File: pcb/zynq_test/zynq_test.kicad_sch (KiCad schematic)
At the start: 0 parts

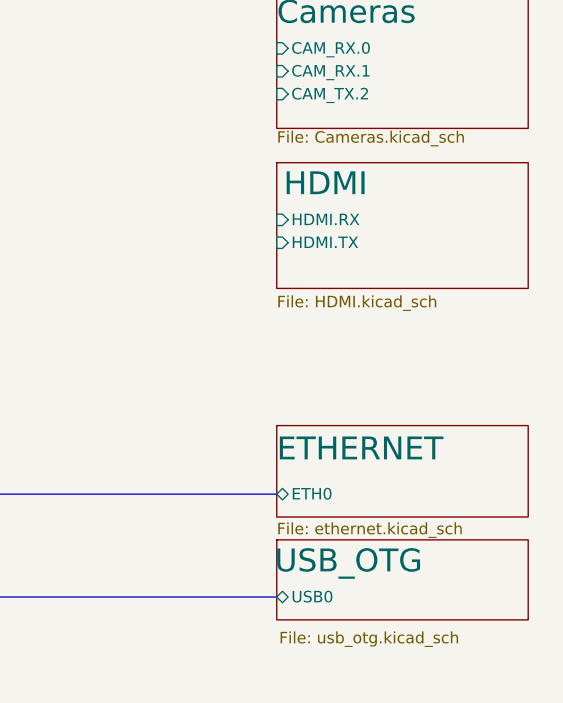
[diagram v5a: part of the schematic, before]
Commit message: Finished HDMI
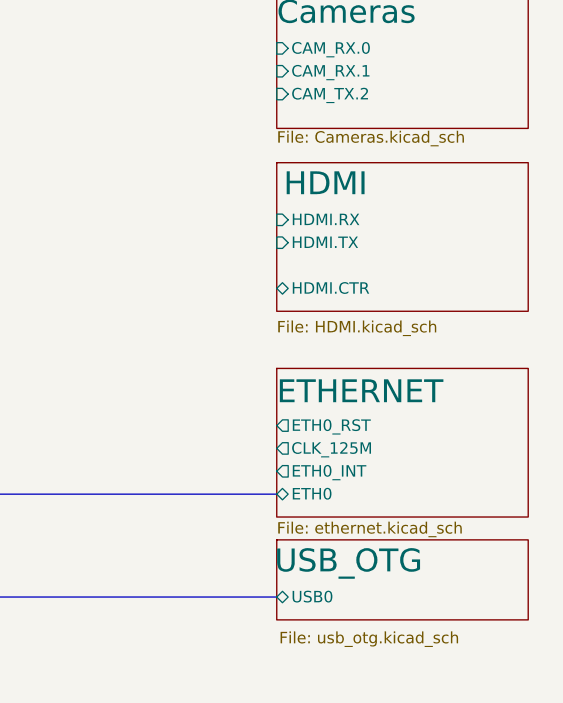
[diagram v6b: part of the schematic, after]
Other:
- sheet ETHERNET ports: added CLK_125M, ETH0_INT, ETH0_RST; removed none
- sheet HDMI ports: added HDMI.CTR; removed none
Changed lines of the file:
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@@
 	(sheet
 		(at 212.09 34.29)
-		(size 27.94 13.97)
+		(size 27.94 16.51)
 		(exclude_from_sim no)
 		(in_bom yes)
@@
 		)
 		(property "Sheetfile" "HDMI.kicad_sch"
-			(at 212.09 49.022 0)
+			(at 212.09 51.816 0)
 			(effects
 				(font
@@
 		(pin "HDMI.TX" input
 			(at 212.09 43.18 180)
+			(effects
+				(font
+					(size 1.27 1.27)
+				)
+				(justify left)
+			)
+		)
+		(pin "HDMI.CTR" bidirectional
+			(at 212.09 48.26 180)
 			(effects
 				(font
@@
 	)
 	(sheet
-		(at 212.09 63.5)
-		(size 27.94 10.16)
+		(at 212.09 57.15)
+		(size 27.94 16.51)
 		(exclude_from_sim no)
 		(in_bom yes)
@@
 		)
 		(property "Sheetname" "ETHERNET"
-			(at 212.09 67.564 0)
+			(at 212.09 61.214 0)
 			(effects
 				(font
@@
 		)
 		(property "Sheetfile" "ethernet.kicad_sch"
-			(at 212.09 74.2446 0)
+			(at 212.09 74.168 0)
 			(effects
 				(font
@@
 			(effects
 				(font
+					(size 1.27 1.27)
+				)
+				(justify left)
+			)
+		)
+		(pin "CLK_125M" output
+			(at 212.09 66.04 180)
+			(effects
+				(font
+					(size 1.27 1.27)
+				)
+				(justify left)
+			)
+		)
+		(pin "ETH0_INT" output
+			(at 212.09 68.58 180)
+			(effects
+				(font
+					(size 1.27 1.27)
+				)
+				(justify left)
+			)
+		)
+		(pin "ETH0_RST" output
+			(at 212.09 63.5 180)
+			(effects
+				(font

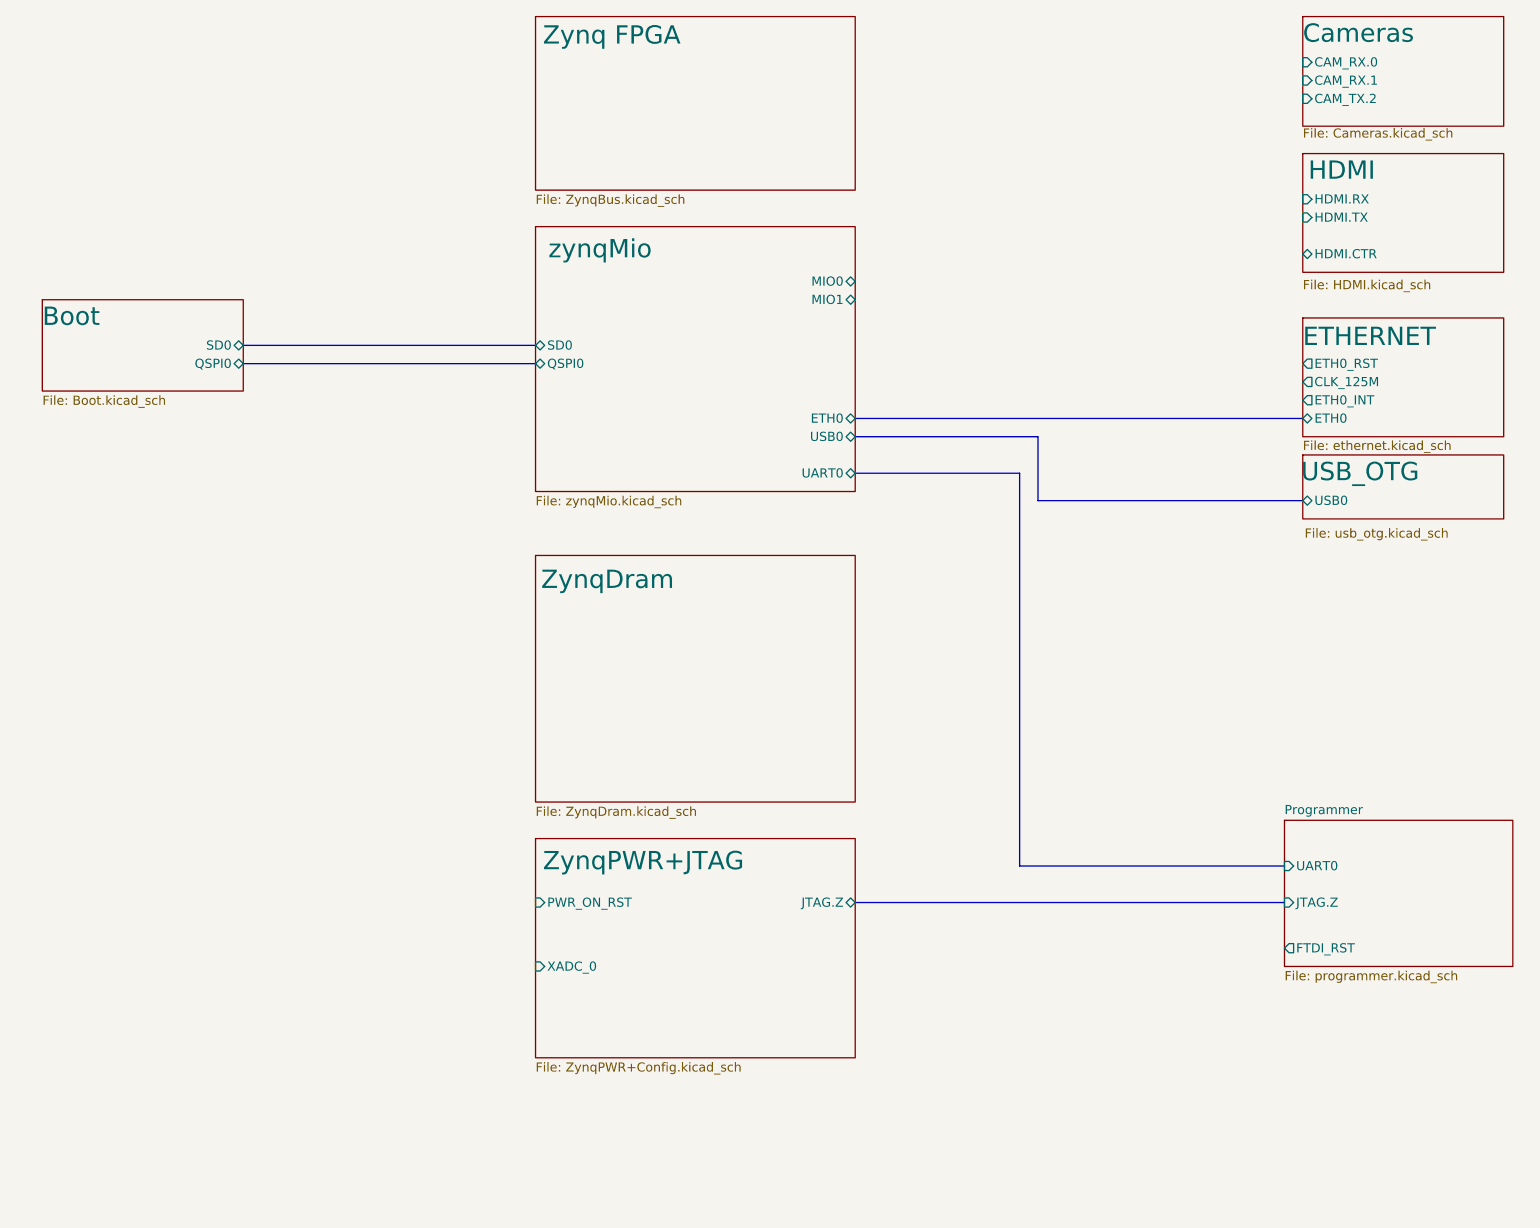
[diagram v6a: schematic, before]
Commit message: Connected DDR3, cleaned up some thing
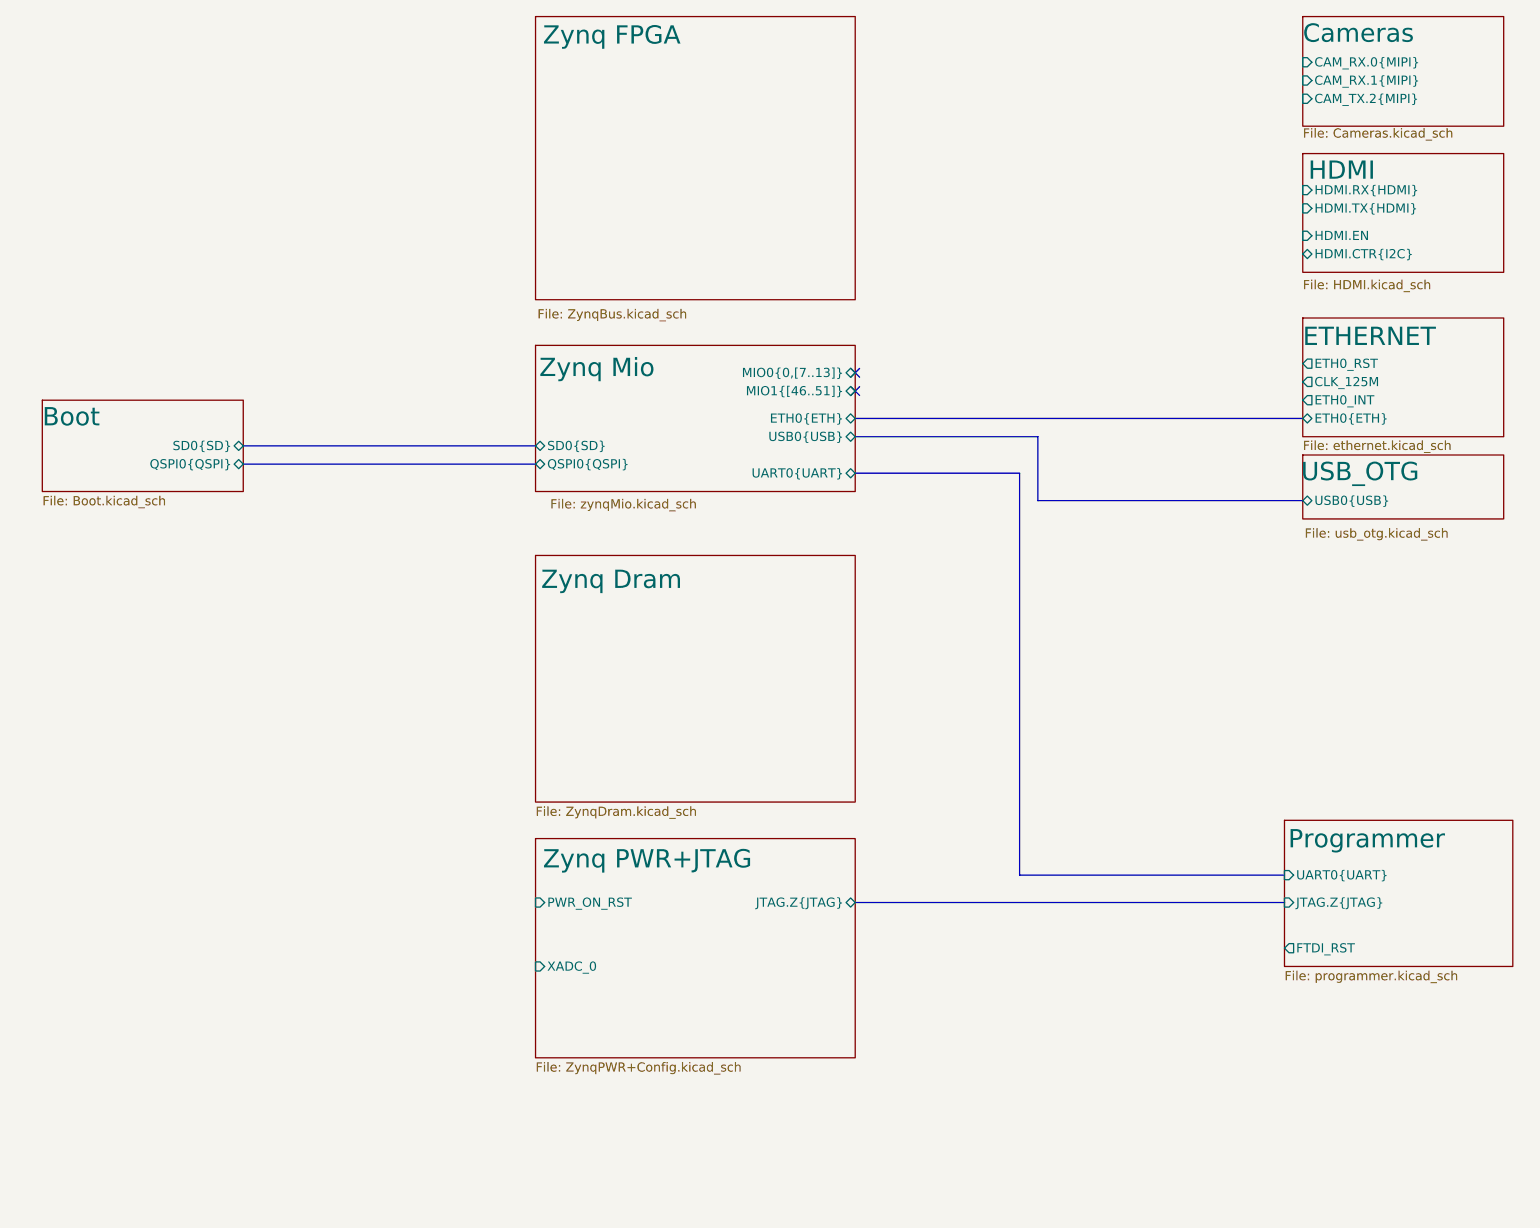
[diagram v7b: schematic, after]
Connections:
- no-connect marks 0 -> 2
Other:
- sheet ZynqDram renamed Zynq Dram
- sheet ZynqPWR+JTAG renamed Zynq PWR+JTAG
- sheet zynqMio renamed Zynq Mio
- sheet Boot ports: added QSPI0{QSPI}, SD0{SD}; removed QSPI0, SD0
- sheet Cameras ports: added CAM_RX.0{MIPI}, CAM_RX.1{MIPI}, CAM_TX.2{MIPI}; removed CAM_RX.0, CAM_RX.1, CAM_TX.2
- sheet ETHERNET ports: added ETH0{ETH}; removed ETH0
- sheet HDMI ports: added HDMI.CTR{I2C}, HDMI.EN, HDMI.RX{HDMI}, HDMI.TX{HDMI}; removed HDMI.CTR, HDMI.RX, HDMI.TX
- sheet Programmer ports: added JTAG.Z{JTAG}, UART0{UART}; removed JTAG.Z, UART0
- sheet USB_OTG ports: added USB0{USB}; removed USB0
- sheet Zynq Mio ports: added ETH0{ETH}, MIO0{0,[7..13]}, MIO1{[46..51]}, QSPI0{QSPI}, SD0{SD}, UART0{UART}, USB0{USB}; removed ETH0, MIO0, MIO1, QSPI0, SD0, UART0, USB0
- sheet Zynq PWR+JTAG ports: added JTAG.Z{JTAG}; removed JTAG.Z

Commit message: Finished Power Supply
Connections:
- no-connect marks 2 -> 15
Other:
- added sheet GPIO (GPIO.kicad_sch)
- added sheet Power (Power.kicad_sch)
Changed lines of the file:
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@@
 	(paper "A4")
 	(title_block
-		(date "2025-09-06")
-		(rev "v1.0")
+		(date "2025-09-13")
+		(rev "A")
+	)
+	(no_connect
+		(at 212.09 41.91)
 	)
 	(no_connect
@@
 	)
 	(no_connect
+		(at 212.09 82.55)
+	)
+	(no_connect
+		(at 209.55 144.78)
+	)
+	(no_connect
+		(at 212.09 48.26)
+	)
+	(no_connect
+		(at 212.09 45.72)
+	)
+	(no_connect
+		(at 212.09 85.09)
+	)
+	(no_connect
 		(at 149.86 64.77)
 	)
-	(bus
-		(pts
-			(xy 175.26 82.55) (xy 175.26 73.66)
+	(no_connect
+		(at 212.09 87.63)
+	)
+	(no_connect
+		(at 105.41 138.43)
+	)
+	(no_connect
+		(at 212.09 39.37)
+	)
+	(no_connect
+		(at 212.09 21.59)
+	)
+	(no_connect
+		(at 212.09 26.67)
+	)
+	(no_connect
+		(at 105.41 147.32)
+	)
+	(no_connect
+		(at 212.09 24.13)
+	)
+	(bus
+		(pts
+			(xy 175.26 101.6) (xy 175.26 73.66)
 		)
 		(stroke
@@
 	(bus
 		(pts
+			(xy 177.8 71.12) (xy 149.86 71.12)
+		)
+		(stroke
+			(width 0)
+			(type default)
+		)
+	)
+	(bus
+		(pts
+			(xy 177.8 90.17) (xy 177.8 71.12)
+		)
+		(stroke
+			(width 0)
+			(type default)
+		)
+	)
+	(bus
+		(pts
 			(xy 172.72 78.74) (xy 172.72 134.62)
 		)
@@
 	(bus
 		(pts
-			(xy 149.86 71.12) (xy 212.09 71.12)
+			(xy 177.8 90.17) (xy 212.09 90.17)
 		)
 		(stroke
@@
 	(bus
 		(pts
-			(xy 175.26 82.55) (xy 212.09 82.55)
+			(xy 175.26 101.6) (xy 212.09 101.6)
 		)
 		(stroke
@@
 	)
 	(sheet
+		(at 33.02 130.81)
+		(size 43.18 25.4)
+		(exclude_from_sim no)
+		(in_bom yes)
+		(on_board yes)
+		(dnp no)
+		(fields_autoplaced yes)
+		(stroke
+			(width 0.1524)
+			(type solid)
+		)
+		(fill
+			(color 0 0 0 0.0000)
+		)
+		(property "Sheetname" "Power"
+			(at 33.02 130.0984 0)
+			(effects
+				(font
+					(size 1.27 1.27)
+				)
+				(justify left bottom)
+			)
+		)
+		(property "Sheetfile" "Power.kicad_sch"
+			(at 33.02 156.7946 0)
+			(effects
+				(font
+					(size 1.27 1.27)
+				)
+				(justify left top)
+			)
+		)
+		(instances
+			(project "zynq_test"
+				(path "/0637578d-4ce5-4d31-b973-2de977269ea5"
+					(page "14")
+				)
+			)
+		)
+	)
+	(sheet
 		(at 105.41 90.17)
 		(size 44.45 34.29)
@@
 	)
 	(sheet
+		(at 212.09 55.88)
+		(size 27.94 16.51)
+		(exclude_from_sim no)
+		(in_bom yes)
+		(on_board yes)
+		(dnp no)
+		(stroke
+			(width 0.1524)
+			(type solid)
+		)
+		(fill
+			(color 0 0 0 0.0000)
+		)
+		(property "Sheetname" "GPIO"
+			(at 212.09 59.69 0)
+			(effects
+				(font
+					(size 2.54 2.54)
+				)
+				(justify left bottom)
+			)
+		)
+		(property "Sheetfile" "GPIO.kicad_sch"
+			(at 212.344 72.898 0)
+			(effects
+				(font
+					(size 1.27 1.27)
+				)
+				(justify left top)
+			)
+		)
+		(instances
+			(project "zynq_test"
+				(path "/0637578d-4ce5-4d31-b973-2de977269ea5"
+					(page "13")
+				)
+			)
+		)
+	)
+	(sheet
 		(at 212.09 34.29)
 		(size 27.94 16.51)
@@
 	)
 	(sheet
-		(at 212.09 57.15)
+		(at 212.09 76.2)
 		(size 27.94 16.51)
 		(exclude_from_sim no)
@@
 		)
 		(property "Sheetname" "ETHERNET"
-			(at 212.09 61.214 0)
+			(at 212.09 80.264 0)
 			(effects
 				(font
@@
 		)
 		(property "Sheetfile" "ethernet.kicad_sch"
-			(at 212.09 74.168 0)
+			(at 212.09 93.218 0)
 			(effects
 				(font
@@
 		)
 		(pin "CLK_125M" output
-			(at 212.09 66.04 180)
+			(at 212.09 85.09 180)
 			(effects
 				(font
@@
 		)
 		(pin "ETH0_INT" output
-			(at 212.09 68.58 180)
+			(at 212.09 87.63 180)
 			(effects
 				(font
@@
 		)
 		(pin "ETH0_RST" output
-			(at 212.09 63.5 180)
+			(at 212.09 82.55 180)
 			(effects
 				(font
@@
 		)
 		(pin "ETH0{ETH}" bidirectional
-			(at 212.09 71.12 180)
+			(at 212.09 90.17 180)
 			(effects
 				(font
@@
 	)
 	(sheet
-		(at 212.09 76.2)
+		(at 212.09 95.25)
 		(size 27.94 8.89)
 		(exclude_from_sim no)
@@
 		)
 		(property "Sheetname" "USB_OTG"
-			(at 211.836 80.01 0)
+			(at 211.836 99.06 0)
 			(effects
 				(font
@@
 		)
 		(property "Sheetfile" "usb_otg.kicad_sch"
-			(at 212.344 86.36 0)
+			(at 212.344 105.41 0)
 			(effects
 				(font
@@
 		)
 		(pin "USB0{USB}" bidirectional
-			(at 212.09 82.55 180)
+			(at 212.09 101.6 180)
 			(effects
 				(font
@@
 	)
 	(embedded_fonts no)
+	(embedded_files
+		(file
+			(name "SheetTemplate.kicad_wks")
+			(type worksheet)
+			(data |KLUv/WB+CMUTADbcWSEAtxsWHGQdlqaixJWgMmfh2tCZyKzY5HXQcxNVVbcAEAFQAEoAUgAh/B3O
+				zZO2eDm5A2l+46HBUjm78+AluXhDg5W0/XTHL/kXAICAICR6H6dUVJrqgq4JQ1Vn/F120TkGjFJq
+				1VlbxHfMPioAAoLxQ9KA3Xc/hV/y995Oy9ae1lTKn3i/85Dn7GLG34c9e1afD4dee/j32zvfoCjC
+				ueuqX3QQCH9dGxS9ziktqxXVkhXrz92PVdUO6sT/PIPwP/YCI7dgWNUQKhEUm1A2zqJlNI2MsUFQ
+				BCvtnAp59TWlwqa0S9bQaBiO21CEXvh3jZyzKfuL/rVpc38UeWxtmpmq7el53qRWAfAi3tC2tUcc
+				qmjVAQGB4bqqtZZEPC5Z5aJpD+5SSEsTclJJNtEimyO8ju+G3d82WEteFENIRNUil+1SKXj73Tvc
+				4JAagFvV34Ey3nT2UFexaJWs4qfLgSH2GlG3jGYJdaAhPaUYmhGRJEkKHYBExMSqG7ZnYf/UXeFb
+				IM2oukJWcjKeZVCGjTWMhUy8XDwRWYjHQURb5Ga0hfkSKue0mhx/YX36Cj3i5k7jAIwo2xZhBro3
+				3UJM24YDkwebfhQeFrxa1f4oKusQJ7gFDGksCLsJASZbNhEyv5f8F9N6PInJsbUuBBQRVByoDeFy
+				JevLuxSpJzWMaOipJyqK1lTks6dcoqx3tGoqDQ1idIc0H6qUvHACH/z2BfdoKcFOmzVa7aKX/pxu
+				Us+lXRAQQiqSU4KpmjACDAjkRIe0IQ0F66JHi1cRBg7mMtNBZR4rOUlqRU4GEwnkdE7s7XRoUefq
+				w1j/C89DpJds9CEdA1EF|
+			)
+			(checksum "F72A94913C597F4C21E195BABBAA6AB8")
+		)
+		(file
+			(name "SheetTemplate2.kicad_wks")
+			(type worksheet)
+			(data |KLUv/WB+COUTAJbcWiEAtxsWHGQdlqaixJWgMmfh2tCZyKzY5HXQcxNVVbcAEAFSAEsAVADYC+Hv
+				cG6etMXLyR1I8xsPDZbK2Z0HL8nFGxqspO2nO37JvwAABAQh0fs4paLSVBd0TRiqOuPvsovOMWCU
+				UqvO2iK+Y/ZRARAQjB+SBuy++ykEFa36S/7e22nZ2tOaSvkT73ce8pxdzPj7sGfP6vPh0GsP/357
+				5xsURTh3XfWLDgLhr2uDotc5pWW1olqyYv25+7Gq2kGd+J9nEP4PiLplNMvILRhWNYRKBMUmlI2z
+				aBlNI2NsEBTBSjunQl59TamwKe2SNTQahuM2FKEX/l0j52zK/qJ/bdrcH0UeW5tmpmp7ep43qVUA
+				vIg3tG3tEYcCAYHhuqq1lkQ8LlnlomkP7lJISxNyUk2STbTI5giv47th97cNFJNWpROTCERf0tIi
+				l+1SKXj73Tvc4JAagFvV34Ey3nT2UFexaJWs4qfLgSH2OnWgIT2lGBoZkSRJCh2ARMTEqhu2Z2H/
+				1F3hWyDNqLpCVnIynmVQho01jIVMvFw8EVmIx0FEW+TILiLsQqhiTsvK8ReuT5/Qs2jubByoEWVg
+				Eaagm6ZbxbSdODB5sOlH4WHBq1Xtj6KyDnGCW8CQxoKwmxBgsmUTIfN7yX8xrceTmBxb60JAEUHF
+				gdoQLleyvrxLkXpSw4iGnnqiomhNRT57yiXKekerptLQIEZ3SPOhSskLJ/DBb19wj5YS7LRZw2pn
+				vvTndJN6Lu2CgBBSkZwSTNWEEWBAICc6pA1pKFgXPVq8ijBwMJeZDkrm2ZKbpPbmZDCRQE7nxN5O
+				hxZ1rj6M9b/wPER6yUYf0jEQVQ==|
+			)
+			(checksum "9584786EC5C298BD25CAC6C84A54774E")
+		)
+		(file
+			(name "SheetTemplate3.kicad_wks")
+			(type worksheet)
+			(data |KLUv/WB+CMUTACacWSEAtxsWHGQdlqaixFXh71gD3OU5ocDu5XXQcxNVVbcAEAFQAEoAUgAh/B3O
+				zZO2eDm5A3G/8dBgqZzdefCSXLyhwUrafrrjl/wLAEBAEBK9j1MuKq66oHNhqOqMv8suOsdwUUqt
+				OmuL+I7ZRwVAQDB+SBzYffdTCF/y995Oy9ae1lTKn3i/85Dn7GLG34c9e1afD4dee/j32zvfoCjC
+				ueuqX3QQCH9dGxS9ziktqxfVkvXqz92PVdUO6sT/PIPwP/YCI79cV9URKhH0olS07ZJpOAfW0CIo
+				gpV2zoVMdGLKhU1lGMzBZZlt01CEZvh3jpyzKfuL/rVpc38UeWxtipmq7el53qRWAfAi3tC2tUcc
+				qmjVAQGBIVGttSQCgsEsmCyDbImFtFQhJ51glEyiPcL7+G7Y/W3DNaWlF0IiaibBaJhKwdvv3tkG
+				h9QA1Kr+DpTxprOHOssls2AWP90NDLHXiKppskt2oCE9pRiaEZEkSQodgETExKobPGQ2+H86qvAs
+				kGagsiJWcjGeFVAyjTWMhUy8XDwRWYjHQURb5Ga0hfkSKue0mhx/YX36Cj3i5k7jAIwo2xZhBro3
+				3UJM24YDkwebfhQeFrxa1f4oKusQJ7gFDGksCLsJASZbNhEyv5f8F9N6PInJsbUuBBQRVByoDeFy
+				JevLuxSpJzWMaOipJyqK1lTks6dcoqx3tGoqDQ1idIc0H6qUvHACH/z2BfdoKcFOmzVa7aKX/pxu
+				Us+lXRAQQiqSU4KpmjACDAjkRIe0IQ0F66JHi1cRBg7mMtNBZR4rOUlqRU4GEwnkdE7s7XRoUefq
+				w1j/C89DpJds9CEdA1EF|
+			)
+			(checksum "C4999FFD9CF6A699CD7F3B0330C2196E")
+		)
+		(file
+			(name "backgroundTemplate.kicad_wks")
+			(type worksheet)
+			(data |KLUv/WB+CMUTACacWSEAtxsWHGQdlqaixFXh71gD3OU5ocDu5XXQcxNVVbcAEAFQAEoAUgAh/B3O
+				zZO2eDm5A3G/8dBgqZzdefCSXLyhwUrafrrjl/wLAEBAEBK9j1MuKq66oHNhqOqMv8suOsdwUUqt
+				OmuL+I7ZRwVAQDB+SBzYffdTCF/y995Oy9ae1lTKn3i/85Dn7GLG34c9e1afD4dee/j32zvfoCjC
+				ueuqX3QQCH9dGxS9ziktqxfVkvXqz92PVdUO6sT/PIPwP/YCI79cV9URKhH0olS07ZJpOAfW0CIo
+				gpV2zoVMdGLKhU1lGMzBZZlt01CEZvh3jpyzKfuL/rVpc38UeWxtipmq7el53qRWAfAi3tC2tUcc
+				qmjVAQGBIVGttSQCgsEsmCyDbImFtFQhJ51glEyiPcL7+G7Y/W3DNaWlF0IiaibBaJhKwdvv3tkG
+				h9QA1Kr+DpTxprOHOssls2AWP90NDLHXiKppskt2oCE9pRiaEZEkSQodgETExKobPGQ2+H86qvAs
+				kGagsiJWcjGeFVAyjTWMhUy8XDwRWYjHQURb5Ga0hfkSKue0mhx/YX36Cj3i5k7jAIwo2xZhBro3
+				3UJM24YDkwebfhQeFrxa1f4oKusQJ7gFDGksCLsJASZbNhEyv5f8F9N6PInJsbUuBBQRVByoDeFy
+				JevLuxSpJzWMaOipJyqK1lTks6dcoqx3tGoqDQ1idIc0H6qUvHACH/z2BfdoKcFOmzVa7aKX/pxu
+				Us+lXRAQQiqSU4KpmjACDAjkRIe0IQ0F66JHi1cRBg7mMtNBZR4rOUlqRU4GEwnkdE7s7XRoUefq
+				w1j/C89DpJds9CEdA1EF|
+			)
+			(checksum "C4999FFD9CF6A699CD7F3B0330C2196E")
+		)
+	)
 )
